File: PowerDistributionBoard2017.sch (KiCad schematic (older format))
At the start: 25 parts, among them J1 Main Computer (Jetson), J10 Drive 1, J11 Drive 2, J12 Drive 3, J13 Drive 4, J14 Digger 1, J15 Digger 2, J16 Bucket 1, J17 Bucket 2, J18 MAux 1, J2 IMU, J3 Localization, J4 Second Computer, J5 Aux 1, J6 Aux 2, J7 Aux 3, J8 Main Button, J9 JM Button, K1 Main Relay, K2 Secondary Relay

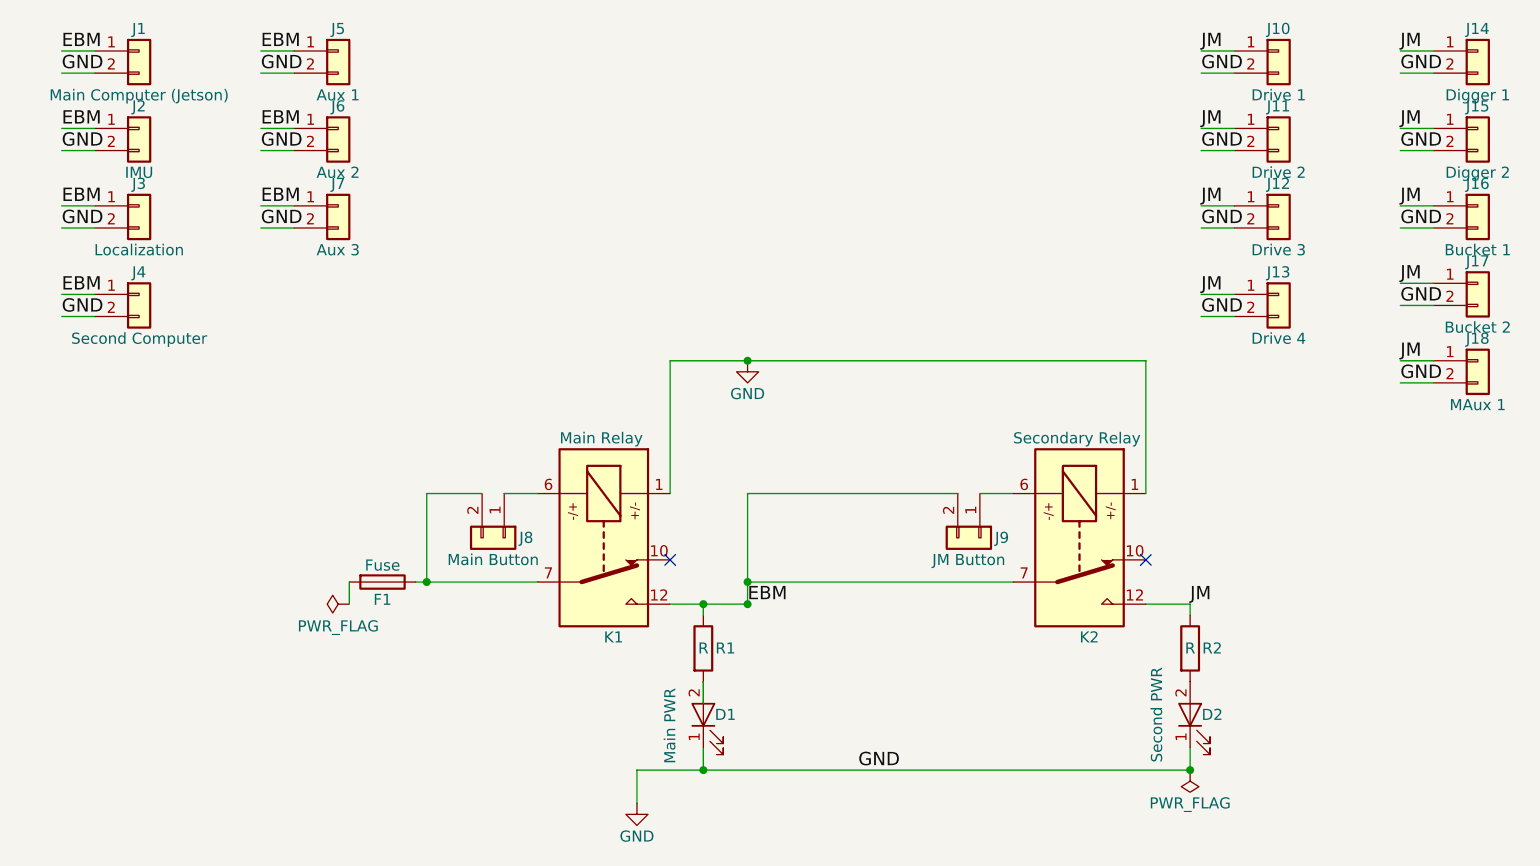
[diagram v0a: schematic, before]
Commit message: battery connector included. part of netlist done
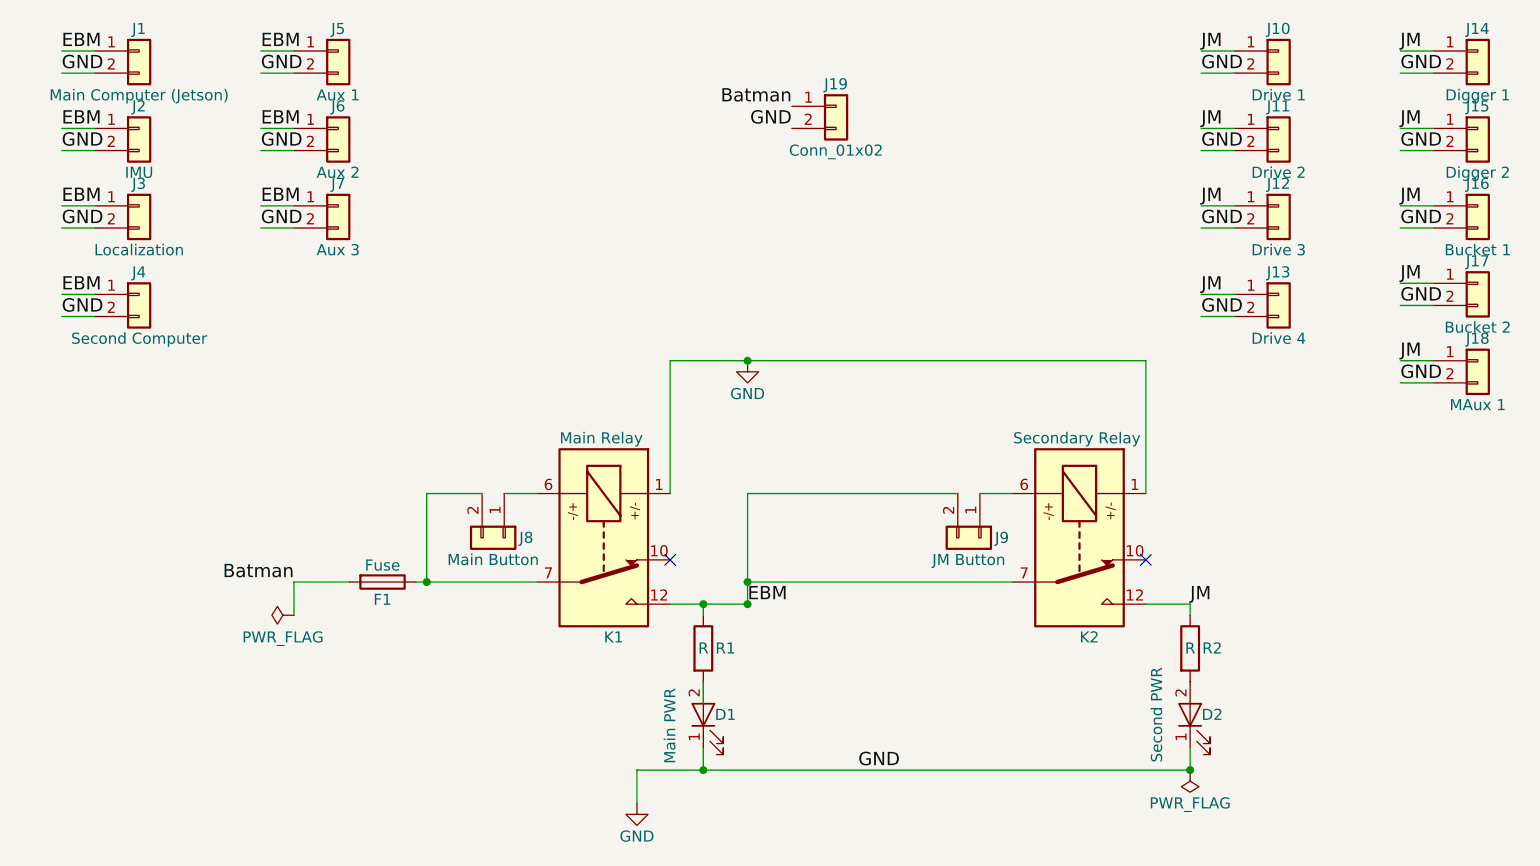
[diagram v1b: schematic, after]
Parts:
- added J19: Conn_01x02, symbol Conn_01x02
- J1, J10, J11, J12, J13, J14, J15, J16, J17, J18, J2, J3, J4, J5, J6, J7: footprint (none) -> Connectors_Molex:Molex_MegaFit_2x01x5.70mm_Angled
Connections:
- net GND: now also J19.2 (Pin_2)
- net Batman: now reaches F1.2
- net Batman: now also J19.1 (Pin_1)
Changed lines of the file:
@@
 L PWR_FLAG #FLG01
 U 1 1 59F399E7
-P 3700 3450
-F 0 "#FLG01" H 3700 3525 50  0001 C CNN
-F 1 "PWR_FLAG" V 3600 3500 50  0000 C CNN
-F 2 "" H 3700 3450 50  0001 C CNN
-F 3 "" H 3700 3450 50  0001 C CNN
-	1    3700 3450
+P 3450 3500
+F 0 "#FLG01" H 3450 3575 50  0001 C CNN
+F 1 "PWR_FLAG" V 3350 3550 50  0000 C CNN
+F 2 "" H 3450 3500 50  0001 C CNN
+F 3 "" H 3450 3500 50  0001 C CNN
+	1    3450 3500
 	0    -1   -1   0
 $EndComp
@@
 $EndComp
 Wire Wire Line
-	3700 3450 3700 3350
+	3450 3350 3450 3500
 Wire Wire Line
 	4000 3350 4550 3350
@@
 F 0 "J1" H 2750 1050 50  0000 C CNN
 F 1 "Main Computer (Jetson)" H 2750 750 50  0000 C CNN
-F 2 "" H 2750 950 50  0001 C CNN
+F 2 "Connectors_Molex:Molex_MegaFit_2x01x5.70mm_Angled" H 2750 950 50  0001 C CNN
 F 3 "" H 2750 950 50  0001 C CNN
 	1    2750 950
@@
 F 0 "J4" H 2750 2150 50  0000 C CNN
 F 1 "Second Computer" H 2750 1850 50  0000 C CNN
-F 2 "" H 2750 2050 50  0001 C CNN
+F 2 "Connectors_Molex:Molex_MegaFit_2x01x5.70mm_Angled" H 2750 2050 50  0001 C CNN
 F 3 "" H 2750 2050 50  0001 C CNN
 	1    2750 2050
@@
 F 0 "J2" H 2750 1400 50  0000 C CNN
 F 1 "IMU" H 2750 1100 50  0000 C CNN
-F 2 "" H 2750 1300 50  0001 C CNN
+F 2 "Connectors_Molex:Molex_MegaFit_2x01x5.70mm_Angled" H 2750 1300 50  0001 C CNN
 F 3 "" H 2750 1300 50  0001 C CNN
 	1    2750 1300
@@
 F 0 "J3" H 2750 1750 50  0000 C CNN
 F 1 "Localization" H 2750 1450 50  0000 C CNN
-F 2 "" H 2750 1650 50  0001 C CNN
+F 2 "Connectors_Molex:Molex_MegaFit_2x01x5.70mm_Angled" H 2750 1650 50  0001 C CNN
 F 3 "" H 2750 1650 50  0001 C CNN
 	1    2750 1650
@@
 F 0 "J5" H 3650 1050 50  0000 C CNN
 F 1 "Aux 1" H 3650 750 50  0000 C CNN
-F 2 "" H 3650 950 50  0001 C CNN
+F 2 "Connectors_Molex:Molex_MegaFit_2x01x5.70mm_Angled" H 3650 950 50  0001 C CNN
 F 3 "" H 3650 950 50  0001 C CNN
 	1    3650 950
@@
 F 0 "J6" H 3650 1400 50  0000 C CNN
 F 1 "Aux 2" H 3650 1100 50  0000 C CNN
-F 2 "" H 3650 1300 50  0001 C CNN
+F 2 "Connectors_Molex:Molex_MegaFit_2x01x5.70mm_Angled" H 3650 1300 50  0001 C CNN
 F 3 "" H 3650 1300 50  0001 C CNN
 	1    3650 1300
@@
 F 0 "J7" H 3650 1750 50  0000 C CNN
 F 1 "Aux 3" H 3650 1450 50  0000 C CNN
-F 2 "" H 3650 1650 50  0001 C CNN
+F 2 "Connectors_Molex:Molex_MegaFit_2x01x5.70mm_Angled" H 3650 1650 50  0001 C CNN
 F 3 "" H 3650 1650 50  0001 C CNN
 	1    3650 1650
@@
 F 0 "J10" H 7900 1050 50  0000 C CNN
 F 1 "Drive 1" H 7900 750 50  0000 C CNN
-F 2 "" H 7900 950 50  0001 C CNN
+F 2 "Connectors_Molex:Molex_MegaFit_2x01x5.70mm_Angled" H 7900 950 50  0001 C CNN
 F 3 "" H 7900 950 50  0001 C CNN
 	1    7900 950
@@
 F 0 "J13" H 7900 2150 50  0000 C CNN
 F 1 "Drive 4" H 7900 1850 50  0000 C CNN
-F 2 "" H 7900 2050 50  0001 C CNN
+F 2 "Connectors_Molex:Molex_MegaFit_2x01x5.70mm_Angled" H 7900 2050 50  0001 C CNN
 F 3 "" H 7900 2050 50  0001 C CNN
 	1    7900 2050
@@
 F 0 "J11" H 7900 1400 50  0000 C CNN
 F 1 "Drive 2" H 7900 1100 50  0000 C CNN
-F 2 "" H 7900 1300 50  0001 C CNN
+F 2 "Connectors_Molex:Molex_MegaFit_2x01x5.70mm_Angled" H 7900 1300 50  0001 C CNN
 F 3 "" H 7900 1300 50  0001 C CNN
 	1    7900 1300
@@
 F 0 "J12" H 7900 1750 50  0000 C CNN
 F 1 "Drive 3" H 7900 1450 50  0000 C CNN
-F 2 "" H 7900 1650 50  0001 C CNN
+F 2 "Connectors_Molex:Molex_MegaFit_2x01x5.70mm_Angled" H 7900 1650 50  0001 C CNN
 F 3 "" H 7900 1650 50  0001 C CNN
 	1    7900 1650
@@
 F 0 "J14" H 8800 1050 50  0000 C CNN
 F 1 "Digger 1" H 8800 750 50  0000 C CNN
-F 2 "" H 8800 950 50  0001 C CNN
+F 2 "Connectors_Molex:Molex_MegaFit_2x01x5.70mm_Angled" H 8800 950 50  0001 C CNN
 F 3 "" H 8800 950 50  0001 C CNN
 	1    8800 950
@@
 F 0 "J15" H 8800 1400 50  0000 C CNN
 F 1 "Digger 2" H 8800 1100 50  0000 C CNN
-F 2 "" H 8800 1300 50  0001 C CNN
+F 2 "Connectors_Molex:Molex_MegaFit_2x01x5.70mm_Angled" H 8800 1300 50  0001 C CNN
 F 3 "" H 8800 1300 50  0001 C CNN
 	1    8800 1300
@@
 F 0 "J16" H 8800 1750 50  0000 C CNN
 F 1 "Bucket 1" H 8800 1450 50  0000 C CNN
-F 2 "" H 8800 1650 50  0001 C CNN
+F 2 "Connectors_Molex:Molex_MegaFit_2x01x5.70mm_Angled" H 8800 1650 50  0001 C CNN
 F 3 "" H 8800 1650 50  0001 C CNN
 	1    8800 1650
@@
 F 0 "J17" H 8800 2100 50  0000 C CNN
 F 1 "Bucket 2" H 8800 1800 50  0000 C CNN
-F 2 "" H 8800 2000 50  0001 C CNN
+F 2 "Connectors_Molex:Molex_MegaFit_2x01x5.70mm_Angled" H 8800 2000 50  0001 C CNN
 F 3 "" H 8800 2000 50  0001 C CNN
 	1    8800 2000
@@
 F 0 "J18" H 8800 2450 50  0000 C CNN
 F 1 "MAux 1" H 8800 2150 50  0000 C CNN
-F 2 "" H 8800 2350 50  0001 C CNN
+F 2 "Connectors_Molex:Molex_MegaFit_2x01x5.70mm_Angled" H 8800 2350 50  0001 C CNN
 F 3 "" H 8800 2350 50  0001 C CNN
 	1    8800 2350
@@
 	-1   0    0    1
 $EndComp
+$Comp
+L Conn_01x02 J19
+U 1 1 59FBCC65
+P 5900 1200
+F 0 "J19" H 5900 1300 50  0000 C CNN
+F 1 "Conn_01x02" H 5900 1000 50  0000 C CNN
+F 2 "" H 5900 1200 50  0001 C CNN
+F 3 "" H 5900 1200 50  0001 C CNN
+	1    5900 1200
+	1    0    0    -1
+$EndComp
+Text Label 5700 1300 2    60   ~ 0
+GND
+Wire Wire Line
+	3450 3350 3700 3350
+Text Label 3450 3350 2    60   ~ 0
+Batman
+Text Label 5700 1200 2    60   ~ 0
+Batman
 $EndSCHEMATC

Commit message: Did stuff
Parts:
- removed J19: Conn_01x02, symbol Conn_01x02
- added J19: Conn_02x02_Counter_Clockwise, Connectors_Molex:Molex_MegaFit_2x02x5.70mm_Angled, symbol Conn_02x02_Counter_Clockwise
- D1: value Main PWR -> Main PWR LED; footprint (none) -> LEDs:LED_1206_HandSoldering
- D2: value Second PWR -> Second PWR LED; footprint (none) -> LEDs:LED_1206_HandSoldering
- F1, J8, J9: footprint (none) -> Connectors_Molex:Molex_MegaFit_2x01x5.70mm_Angled
- R1, R2: footprint (none) -> Resistors_SMD:R_1206_HandSoldering
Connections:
- net Batman: now also J19.1 (Pin_1), J19.2 (Pin_2)
- net GND: now also J19.3 (Pin_3), J19.4 (Pin_4)
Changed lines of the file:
@@
 F 0 "J8" V 4400 3250 50  0000 C CNN
 F 1 "Main Button" V 4500 3100 50  0000 C CNN
-F 2 "" H 4400 3150 50  0001 C CNN
+F 2 "Connectors_Molex:Molex_MegaFit_2x01x5.70mm_Angled" H 4400 3150 50  0001 C CNN
 F 3 "" H 4400 3150 50  0001 C CNN
 	1    4400 3150
@@
 L PWR_FLAG #FLG01
 U 1 1 59F399E7
-P 3450 3500
-F 0 "#FLG01" H 3450 3575 50  0001 C CNN
-F 1 "PWR_FLAG" V 3350 3550 50  0000 C CNN
-F 2 "" H 3450 3500 50  0001 C CNN
-F 3 "" H 3450 3500 50  0001 C CNN
-	1    3450 3500
+P 3400 3450
+F 0 "#FLG01" H 3400 3525 50  0001 C CNN
+F 1 "PWR_FLAG" V 3300 3500 50  0000 C CNN
+F 2 "" H 3400 3450 50  0001 C CNN
+F 3 "" H 3400 3450 50  0001 C CNN
+	1    3400 3450
 	0    -1   -1   0
 $EndComp
@@
 F 0 "F1" V 3930 3350 50  0000 C CNN
 F 1 "Fuse" V 3775 3350 50  0000 C CNN
-F 2 "" V 3780 3350 50  0001 C CNN
+F 2 "Connectors_Molex:Molex_MegaFit_2x01x5.70mm_Angled" V 3780 3350 50  0001 C CNN
 F 3 "" H 3850 3350 50  0001 C CNN
 	1    3850 3350
@@
 F 0 "R1" H 5400 3650 50  0000 C CNN
 F 1 "R" H 5300 3650 50  0000 C CNN
-F 2 "" V 5230 3650 50  0001 C CNN
+F 2 "Resistors_SMD:R_1206_HandSoldering" V 5230 3650 50  0001 C CNN
 F 3 "" H 5300 3650 50  0001 C CNN
 	1    5300 3650
@@
 F 0 "R2" H 7600 3650 50  0000 C CNN
 F 1 "R" H 7500 3650 50  0000 C CNN
-F 2 "" V 7430 3650 50  0001 C CNN
+F 2 "Resistors_SMD:R_1206_HandSoldering" V 7430 3650 50  0001 C CNN
 F 3 "" H 7500 3650 50  0001 C CNN
 	1    7500 3650
@@
 P 5300 3950
 F 0 "D1" V 5300 3850 50  0000 C CNN
-F 1 "Main PWR" H 5250 4100 50  0000 C CNN
-F 2 "" H 5300 3950 50  0001 C CNN
+F 1 "Main PWR LED" H 5250 4100 50  0000 C CNN
+F 2 "LEDs:LED_1206_HandSoldering" H 5300 3950 50  0001 C CNN
 F 3 "" H 5300 3950 50  0001 C CNN
 	1    5300 3950
@@
 P 7500 3950
 F 0 "D2" V 7500 3850 50  0000 C CNN
-F 1 "Second PWR" H 7500 4100 50  0000 C CNN
-F 2 "" H 7500 3950 50  0001 C CNN
+F 1 "Second PWR LED" H 7500 4100 50  0000 C CNN
+F 2 "LEDs:LED_1206_HandSoldering" H 7500 3950 50  0001 C CNN
 F 3 "" H 7500 3950 50  0001 C CNN
 	1    7500 3950
@@
 $EndComp
 Wire Wire Line
-	3450 3350 3450 3500
+	3700 3450 3700 3350
 Wire Wire Line
 	4000 3350 4550 3350
@@
 F 0 "J9" V 6550 3250 50  0000 C CNN
 F 1 "JM Button" V 6650 3100 50  0000 C CNN
-F 2 "" H 6550 3150 50  0001 C CNN
+F 2 "Connectors_Molex:Molex_MegaFit_2x01x5.70mm_Angled" H 6550 3150 50  0001 C CNN
 F 3 "" H 6550 3150 50  0001 C CNN
 	1    6550 3150
@@
 NoConn ~ 7300 3250
 $Comp
+L Conn_02x02_Counter_Clockwise J19
+U 1 1 59FE3500
+P 5900 1500
+F 0 "J19" H 5950 1600 50  0000 C CNN
+F 1 "Conn_02x02_Counter_Clockwise" H 5950 1300 50  0000 C CNN
+F 2 "Connectors_Molex:Molex_MegaFit_2x02x5.70mm_Angled" H 5900 1500 50  0001 C CNN
+F 3 "" H 5900 1500 50  0001 C CNN
+	1    5900 1500
+	1    0    0    -1
+$EndComp
+Text Label 3400 3450 0    60   ~ 0
+Batman
+Wire Wire Line
+	3700 3450 3400 3450
+Text Label 5700 1500 2    60   ~ 0
+Batman
+Text Label 5700 1600 2    60   ~ 0
+Batman
+Text Label 6200 1500 0    60   ~ 0
+GND
+Text Label 6200 1600 0    60   ~ 0
+GND
+$Comp
 L PWR_FLAG #FLG04
-U 1 1 59FB8A4A
+U 1 1 59FE54B1
 P 7500 4200
 F 0 "#FLG04" H 7500 4275 50  0001 C CNN
@@
 	-1   0    0    1
 $EndComp
-$Comp
-L Conn_01x02 J19
-U 1 1 59FBCC65
-P 5900 1200
-F 0 "J19" H 5900 1300 50  0000 C CNN
-F 1 "Conn_01x02" H 5900 1000 50  0000 C CNN
-F 2 "" H 5900 1200 50  0001 C CNN
-F 3 "" H 5900 1200 50  0001 C CNN
-	1    5900 1200
-	1    0    0    -1
-$EndComp
-Text Label 5700 1300 2    60   ~ 0
-GND
-Wire Wire Line
-	3450 3350 3700 3350
-Text Label 3450 3350 2    60   ~ 0
-Batman
-Text Label 5700 1200 2    60   ~ 0
-Batman
 $EndSCHEMATC
